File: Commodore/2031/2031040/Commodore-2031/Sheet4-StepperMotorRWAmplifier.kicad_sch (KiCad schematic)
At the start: 86 parts, among them Q1 2N4401, Q2 2N4400, Q3 2N4403, Q4 2N4403, Q5 2N4403

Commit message: Work towards ERC
- Add power flags
- Try to make sense of ground symbols
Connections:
- net GND renamed 12V_GND
- net 12V_GND: no longer C51.2
- net GNDPWR renamed Earth
- net Earth: now also C51.2
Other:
- moved on the sheet: R24

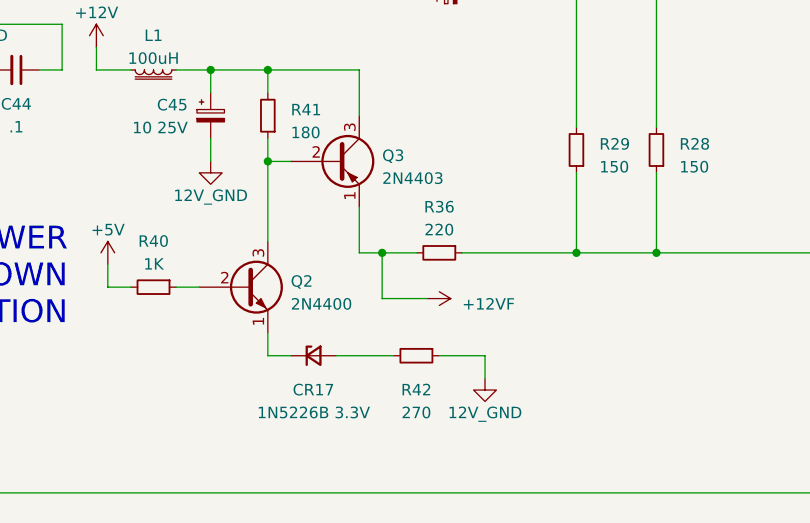
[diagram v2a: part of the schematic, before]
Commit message: Resolve remaining ERC errors
... still lots of warnings tho.
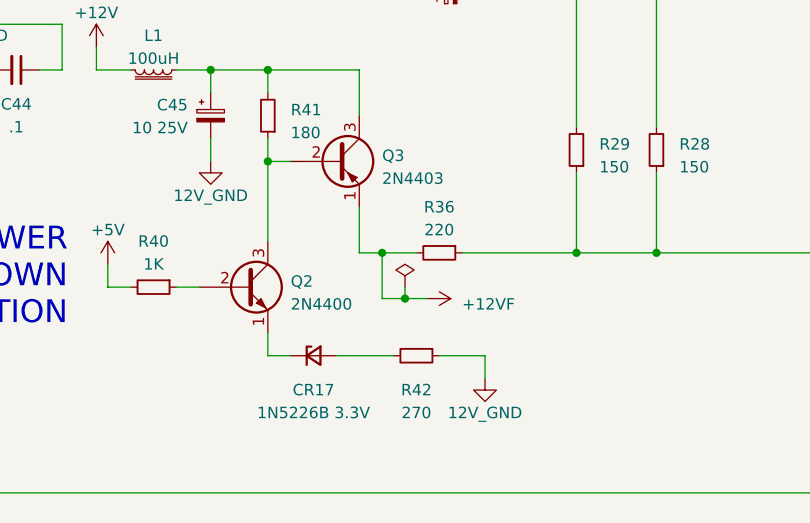
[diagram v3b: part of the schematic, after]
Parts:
- UR2: symbol Comparator:LM311 -> Commodore-2031:311
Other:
- title: (none) -> Stepper Motor & R/W Amplifier
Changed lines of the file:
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@@
 (kicad_sch (version 20230121) (generator eeschema)
   (paper "A3")
+  (title_block
+    (title "Stepper Motor & R/W Amplifier")
+    (comment 1 "Schematic 203138")
+    (comment 2 "PCB Assembly 2031040")
+    (comment 4 "captured from original service manual by @rjhelms")
+  )
   (junction (at 247.65 238.76) (diameter 0) (color 0 0 0 0)
   )
@@
   )
   (junction (at 212.09 229.87) (diameter 0) (color 0 0 0 0)
+  )
+  (junction (at 142.24 234.95) (diameter 0) (color 0 0 0 0)
   )
   (junction (at 274.32 109.22) (diameter 0) (color 0 0 0 0)
@@
     (stroke (width 0) (type default))
   )
+  (wire (pts (xy 142.24 233.68) (xy 142.24 234.95))
+    (stroke (width 0) (type default))
+  )
   (wire (pts (xy 262.89 125.73) (xy 267.97 125.73))
     (stroke (width 0) (type default))
@@
     (stroke (width 0) (type default))
   )
+  (wire (pts (xy 142.24 234.95) (xy 144.78 234.95))
+    (stroke (width 0) (type default))
+  )
   (wire (pts (xy 121.92 82.55) (xy 121.92 83.82))
     (stroke (width 0) (type default))
@@
     (stroke (width 0) (type default))
   )
-  (wire (pts (xy 139.7 234.95) (xy 144.78 234.95))
+  (wire (pts (xy 139.7 234.95) (xy 142.24 234.95))
     (stroke (width 0) (type default))
   )
@@
     )
   )
-  (symbol (lib_id "Comparator:LM311") (at 257.81 139.7 0) (unit 1)
+  (symbol (lib_id "Commodore-2031:311") (at 257.81 139.7 0) (unit 1)
     (in_bom yes) (on_board yes) (dnp no) (fields_autoplaced)
     (property "Reference" "UR2" (at 266.7 136.2711 0)
@@
         )
       )
+    )
+  )
+  (symbol (lib_id "power:PWR_FLAG") (at 142.24 233.68 0) (unit 1)
+    (in_bom yes) (on_board yes) (dnp no) (fields_autoplaced)
+    (property "Reference" "#FLG08" (at 142.24 231.775 0)
+      (effects (font (size 1.27 1.27)) hide)
+    )
+    (property "Value" "PWR_FLAG" (at 142.24 229.87 0)
+      (effects (font (size 1.27 1.27)) hide)
+    )
+    (property "Footprint" "" (at 142.24 233.68 0)
+      (effects (font (size 1.27 1.27)) hide)
+    )
+    (property "Datasheet" "~" (at 142.24 233.68 0)
+      (effects (font (size 1.27 1.27)) hide)
+    )
+    (pin "1")
+    (instances
+      (project "Commodore-2031"
+        (path "/4559151c-aecb-4a2a-972f-dcb7dcb5a3dc/a976448e-b270-4ea7-bfe5-2f24cb6d757c"
+          (reference "#FLG08") (unit 1)
+        )
+      )

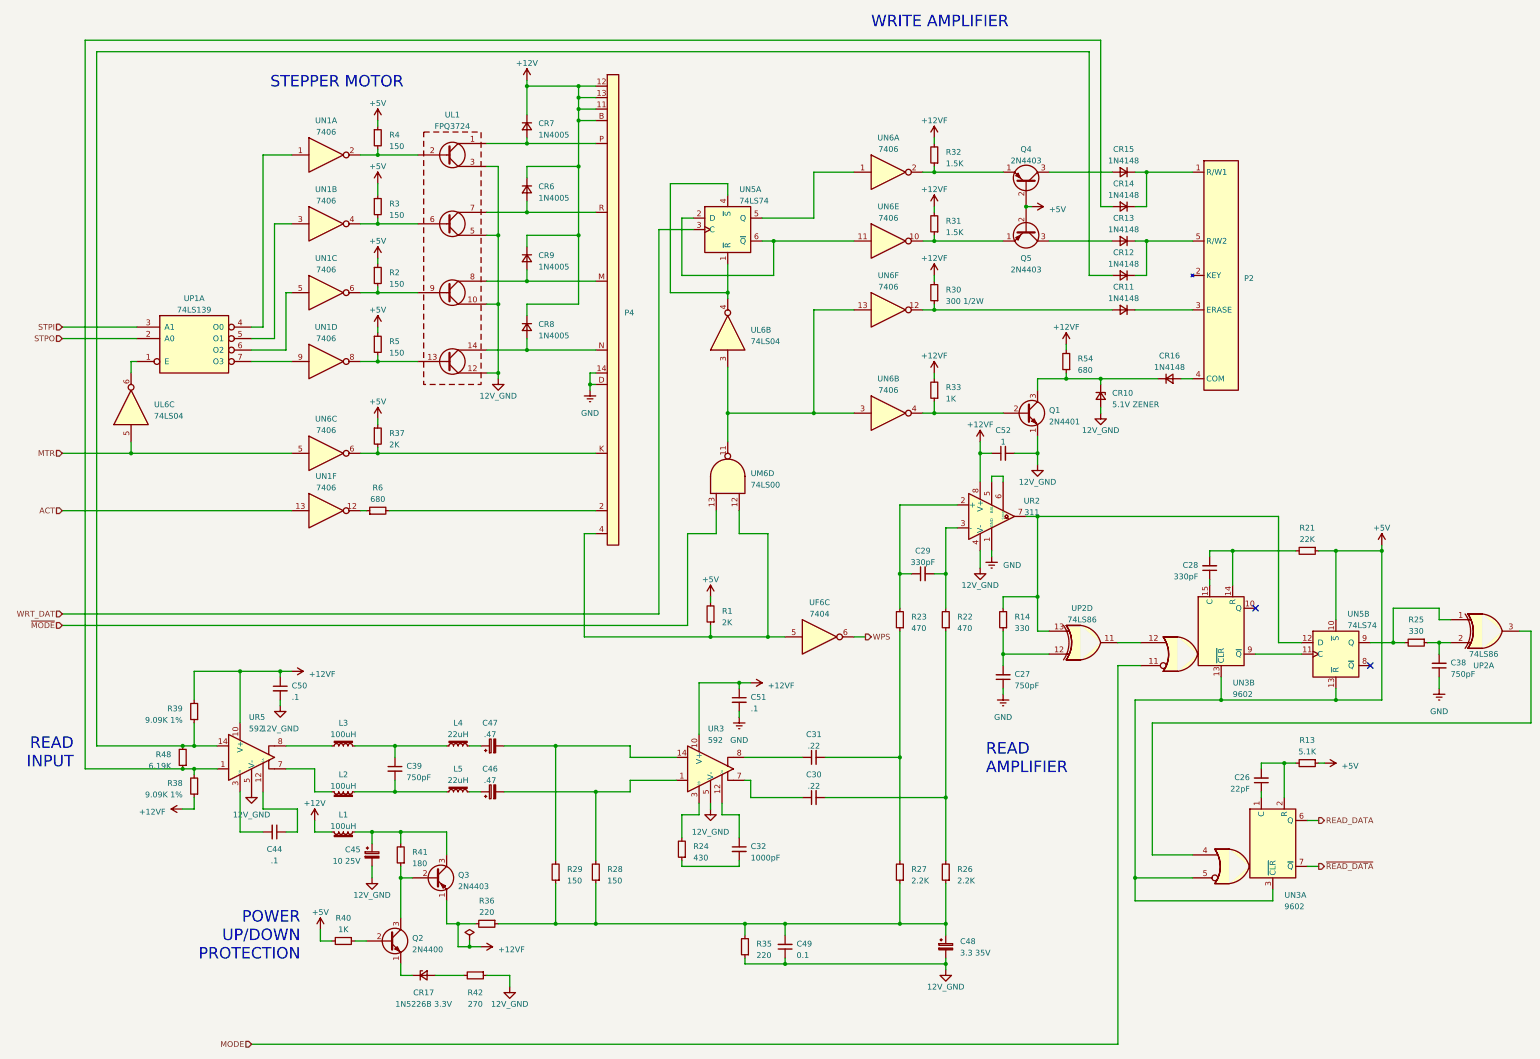
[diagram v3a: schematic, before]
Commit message: Verify schematic against parts list
A few discrepancies appear in original, these are noted in schematic.
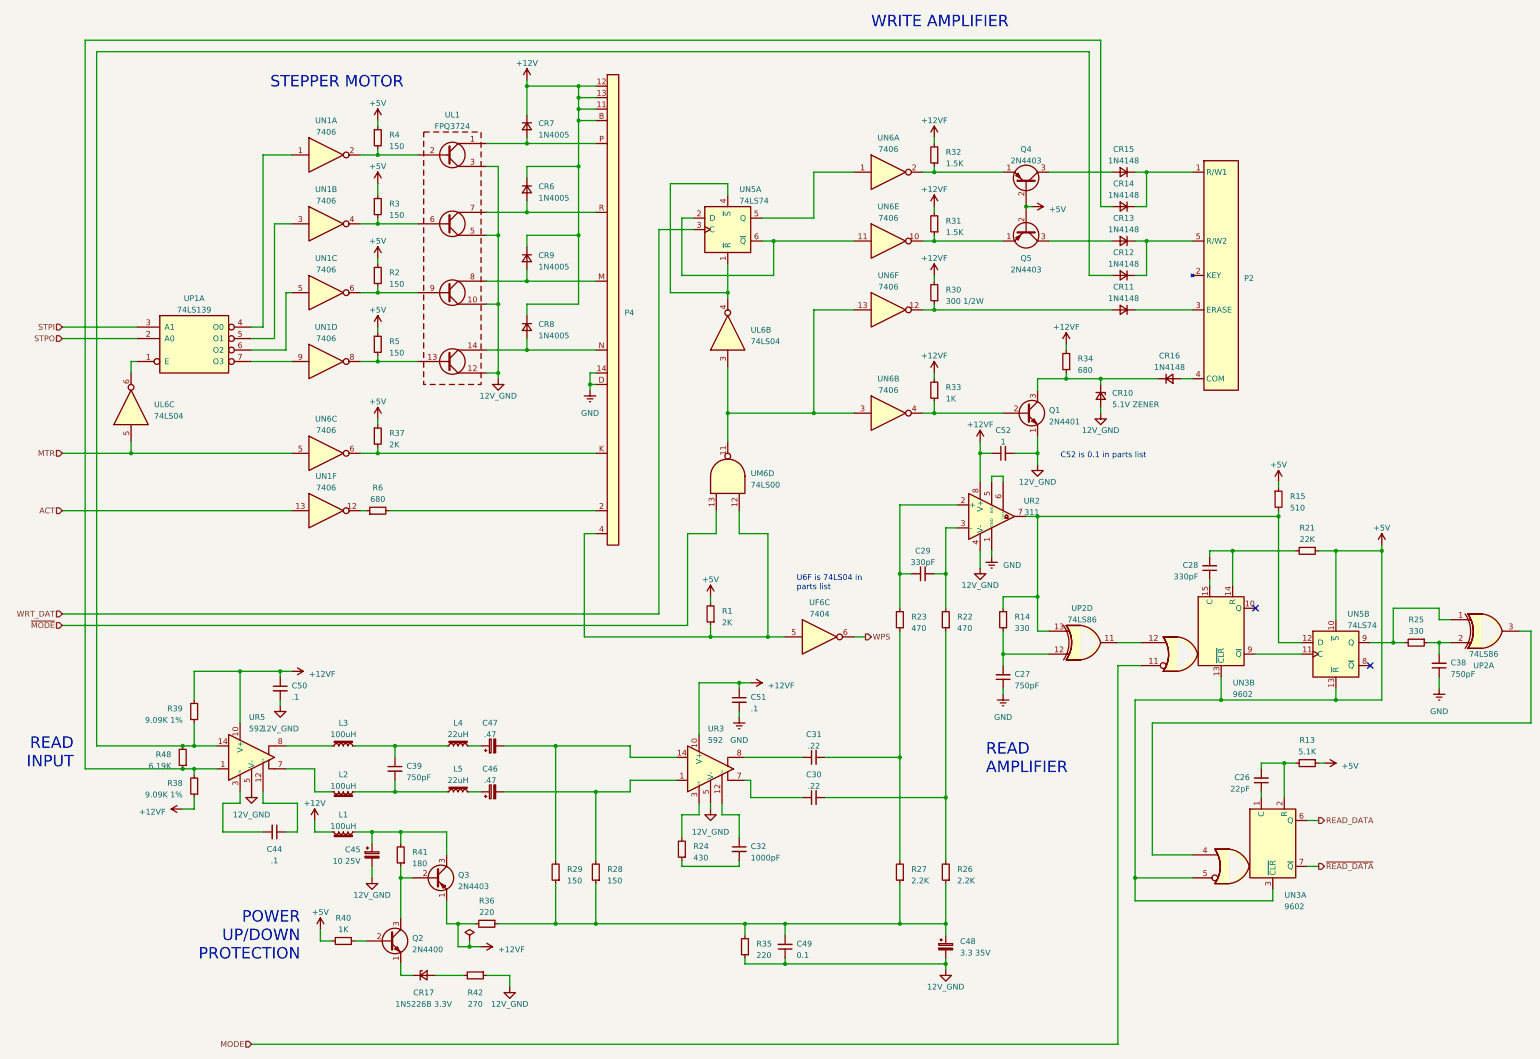
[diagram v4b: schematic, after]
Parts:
- added R15: 510, symbol Device:R_Small
- renumbered R54 to R34
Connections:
- net +5V: now also R15.1
- net at R14.2, UN5.12 (D), UP2.13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: now also R15.2
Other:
- note added: "C52 is 0.1 in parts list"
- note added: "U6F is 74LS04 in parts list"
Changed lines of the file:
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@@
   (junction (at 209.55 78.74) (diameter 0) (color 0 0 0 0)
   )
+  (junction (at 321.31 139.7) (diameter 0) (color 0 0 0 0)
+  )
   (junction (at 247.65 201.93) (diameter 0) (color 0 0 0 0)
   )
@@
     (stroke (width 0) (type default))
   )
+  (wire (pts (xy 91.44 203.2) (xy 91.44 200.66))
+    (stroke (width 0) (type default))
+  )
   (wire (pts (xy 116.84 200.66) (xy 125.73 200.66))
     (stroke (width 0) (type default))
@@
     (stroke (width 0) (type default))
   )
+  (wire (pts (xy 87.63 203.2) (xy 91.44 203.2))
+    (stroke (width 0) (type default))
+  )
   (wire (pts (xy 247.65 229.87) (xy 237.49 229.87))
     (stroke (width 0) (type default))
@@
     (stroke (width 0) (type default))
   )
-  (wire (pts (xy 96.52 204.47) (xy 96.52 200.66))
+  (wire (pts (xy 96.52 203.2) (xy 96.52 200.66))
     (stroke (width 0) (type default))
   )
@@
     (stroke (width 0) (type default))
   )
-  (wire (pts (xy 91.44 200.66) (xy 91.44 209.55))
+  (wire (pts (xy 87.63 203.2) (xy 87.63 209.55))
     (stroke (width 0) (type default))
   )
@@
     (stroke (width 0) (type default))
   )
+  (wire (pts (xy 321.31 138.43) (xy 321.31 139.7))
+    (stroke (width 0) (type default))
+  )
   (wire (pts (xy 193.04 205.74) (xy 193.04 203.2))
     (stroke (width 0) (type default))
@@
     (stroke (width 0) (type default))
   )
-  (wire (pts (xy 104.14 209.55) (xy 104.14 204.47))
+  (wire (pts (xy 104.14 209.55) (xy 104.14 203.2))
     (stroke (width 0) (type default))
   )
@@
     (stroke (width 0) (type default))
   )
-  (wire (pts (xy 91.44 209.55) (xy 96.52 209.55))
+  (wire (pts (xy 87.63 209.55) (xy 96.52 209.55))
     (stroke (width 0) (type default))
   )
@@
     (stroke (width 0) (type default))
   )
-  (wire (pts (xy 104.14 204.47) (xy 96.52 204.47))
+  (wire (pts (xy 104.14 203.2) (xy 96.52 203.2))
     (stroke (width 0) (type default))
   )
@@
     (stroke (width 0) (type default))
   )
+  (wire (pts (xy 321.31 132.08) (xy 321.31 133.35))
+    (stroke (width 0) (type default))
+  )
   (wire (pts (xy 139.7 229.87) (xy 137.16 229.87))
     (stroke (width 0) (type default))
@@
     (stroke (width 0) (type default))
   )
+  (text "C52 is 0.1 in parts list" (at 273.05 127 0)
+    (effects (font (size 1.27 1.27)) (justify left bottom))
+  )
   (text "STEPPER MOTOR" (at 127.635 45.085 0)
     (effects (font (size 2.54 2.54)) (justify right bottom))
@@
     (effects (font (size 2.54 2.54)) (justify left bottom))
   )
+  (text "U6F is 74LS04 in\nparts list" (at 214.63 156.21 0)
+    (effects (font (size 1.27 1.27)) (justify left bottom))
+  )
   (text "WRITE AMPLIFIER" (at 231.14 31.75 0)
     (effects (font (size 2.54 2.54)) (justify left bottom))
@@
     )
   )
+  (symbol (lib_id "power:+5V") (at 321.31 132.08 0) (unit 1)
+    (in_bom yes) (on_board yes) (dnp no) (fields_autoplaced)
+    (property "Reference" "#PWR0119" (at 321.31 135.89 0)
+      (effects (font (size 1.27 1.27)) hide)
+    )
+    (property "Value" "+5V" (at 321.31 128.27 0)
+      (effects (font (size 1.27 1.27)))
+    )
+    (property "Footprint" "" (at 321.31 132.08 0)
+      (effects (font (size 1.27 1.27)) hide)
+    )
+    (property "Datasheet" "" (at 321.31 132.08 0)
+      (effects (font (size 1.27 1.27)) hide)
+    )
+    (pin "1")
+    (instances
+      (project "Commodore-2031"
+        (path "/4559151c-aecb-4a2a-972f-dcb7dcb5a3dc/a976448e-b270-4ea7-bfe5-2f24cb6d757c"
+          (reference "#PWR0119") (unit 1)
+        )
+      )
+    )
+  )
   (symbol (lib_name "9602_1") (lib_id "Commodore-2031:9602") (at 308.61 165.1 0) (unit 2)
     (in_bom yes) (on_board yes) (dnp no) (fields_autoplaced)
@@
     )
   )
+  (symbol (lib_id "Device:R_Small") (at 321.31 135.89 0) (unit 1)
+    (in_bom yes) (on_board yes) (dnp no) (fields_autoplaced)
+    (property "Reference" "R15" (at 323.85 135.255 0)
+      (effects (font (size 1.27 1.27)) (justify left))
+    )
+    (property "Value" "510" (at 323.85 137.795 0)
+      (effects (font (size 1.27 1.27)) (justify left))
+    )
+    (property "Footprint" "" (at 321.31 135.89 0)
+      (effects (font (size 1.27 1.27)) hide)
+    )
+    (property "Datasheet" "~" (at 321.31 135.89 0)
+      (effects (font (size 1.27 1.27)) hide)
+    )
+    (pin "1")
+    (pin "2")
+    (instances
+      (project "Commodore-2031"
+        (path "/4559151c-aecb-4a2a-972f-dcb7dcb5a3dc/a976448e-b270-4ea7-bfe5-2f24cb6d757c"
+          (reference "R15") (unit 1)
+        )
+      )
+    )
+  )
   (symbol (lib_id "Device:Q_NPN_EBC") (at 124.46 233.68 0) (unit 1)
     (in_bom yes) (on_board yes) (dnp no) (fields_autoplaced)
@@
   (symbol (lib_id "Device:R_Small") (at 274.32 105.41 180) (unit 1)
     (in_bom yes) (on_board yes) (dnp no)
-    (property "Reference" "R54" (at 276.86 104.775 0)
+    (property "Reference" "R34" (at 276.86 104.775 0)
       (effects (font (size 1.27 1.27)) (justify right))
     )
@@
       (project "Commodore-2031"
         (path "/4559151c-aecb-4a2a-972f-dcb7dcb5a3dc/a976448e-b270-4ea7-bfe5-2f24cb6d757c"
-          (reference "R54") (unit 1)
+          (reference "R34") (unit 1)
         )
       )
